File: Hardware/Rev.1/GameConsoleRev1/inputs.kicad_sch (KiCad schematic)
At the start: 7 parts, among them J8 Inputs, J9 Button Pulls

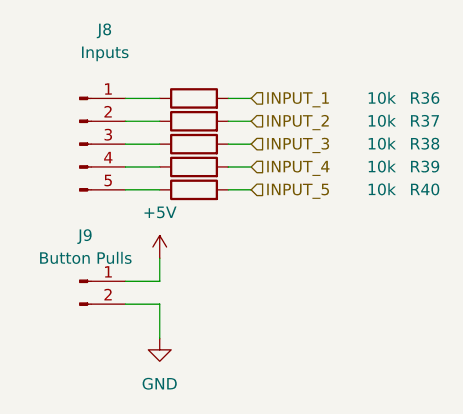
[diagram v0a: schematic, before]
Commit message: Added CPP Build
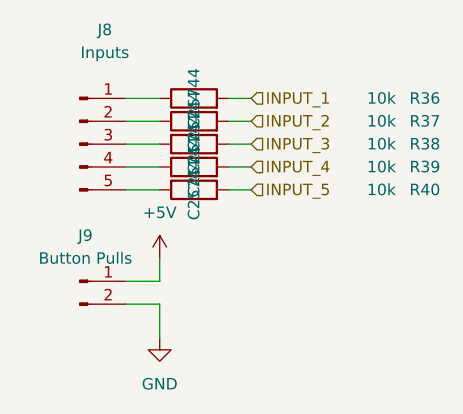
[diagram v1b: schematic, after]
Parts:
- R36, R37, R38, R39, R40: LCSC (none) -> C25744
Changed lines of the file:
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@@
+			)
+		)
+		(property "DK" ""
+			(at 91.44 69.85 0)
+			(effects
+				(font
+					(size 1.27 1.27)
+				)
 			)
 		)
@@
 			)
 		)
+		(property "DK" ""
+			(at 104.14 59.69 0)
+			(effects
+				(font
+					(size 1.27 1.27)
+				)
+			)
+		)
+		(property "LCSC" "C25744"
+			(at 104.14 59.69 0)
+			(effects
+				(font
+					(size 1.27 1.27)
+				)
+			)
+		)
 		(pin "1"
 		)
@@
 			)
 		)
+		(property "DK" ""
+			(at 104.14 52.07 0)
+			(effects
+				(font
+					(size 1.27 1.27)
+				)
+			)
+		)
+		(property "LCSC" "C25744"
+			(at 104.14 52.07 0)
+			(effects
+				(font
+					(size 1.27 1.27)
+				)
+			)
+		)
 		(pin "1"
 		)
@@
 			)
 		)
+		(property "DK" ""
+			(at 104.14 54.61 0)
+			(effects
+				(font
+					(size 1.27 1.27)
+				)
+			)
+		)
+		(property "LCSC" "C25744"
+			(at 104.14 54.61 0)
+			(effects
+				(font
+					(size 1.27 1.27)
+				)
+			)
+		)
 		(pin "1"
 		)
@@
 			)
 		)
+		(property "DK" ""
+			(at 104.14 57.15 0)
+			(effects
+				(font
+					(size 1.27 1.27)
+				)
+			)
+		)
+		(property "LCSC" "C25744"
+			(at 104.14 57.15 0)
+			(effects
+				(font
+					(size 1.27 1.27)
+				)
+			)
+		)
 		(pin "1"
 		)
@@
 				)
 				(hide yes)
+			)
+		)
+		(property "DK" ""
+			(at 104.14 49.53 0)
+			(effects
+				(font
+					(size 1.27 1.27)
+				)
+			)
+		)
+		(property "LCSC" "C25744"
+			(at 104.14 49.53 0)
+			(effects
+				(font
+					(size 1.27 1.27)
+				)
 			)
 		)
@@
 			)
 		)
+		(property "DK" ""
+			(at 91.44 54.61 0)
+			(effects
+				(font
+					(size 1.27 1.27)
+				)
+			)
+		)
